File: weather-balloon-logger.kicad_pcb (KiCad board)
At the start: 2 copper layers, 30 x 20 mm, 0 parts

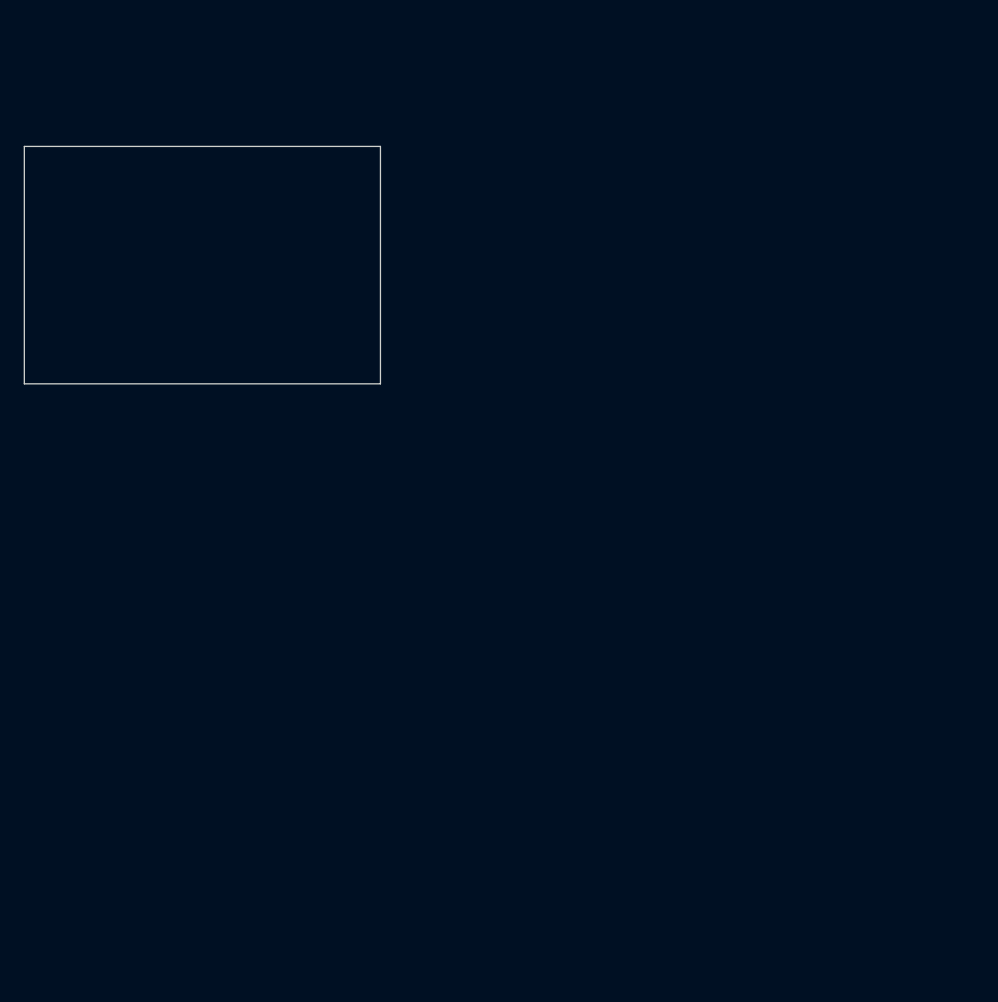
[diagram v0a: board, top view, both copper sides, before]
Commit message: copperhead: create pipeline stage: layout-draft
Completed pipeline stage layout-draft. The 80 × 70 mm PCB contains explicit coordinates for all 15 refdes, edge-located connectors, local OpenLog decoupling, compact LED and cutdown clusters, dual 5 mm SMA clearance envelopes, reserved ESD areas, and DRC-clean routing for power, ground, RF, UART/LED, decoupling, and cutdown nets. LAYOUT.md includes the required `## Draft quality` section with precise acceptable work and mandatory specialist rework. Final verification: ERC clean, DRC clean, BOM/PINOUT drift clean, and board SVG exported. Pre-fabrication holds remain explicitly documented: replace board-local placeholder land patterns, enforce RF rule areas, design 50 Ω launches from a real stackup, capture qualified ESD parts, and complete mechanical/thermal review.

Verification: ERC clean, DRC clean
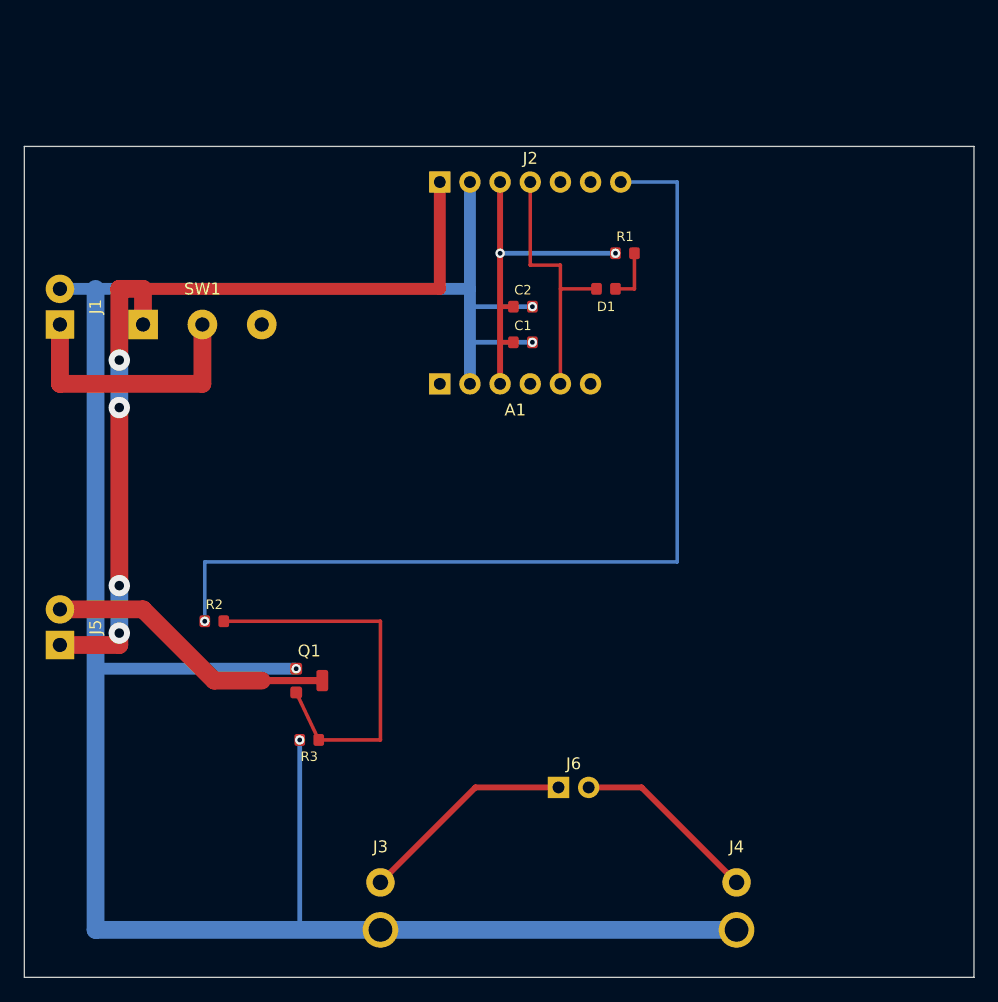
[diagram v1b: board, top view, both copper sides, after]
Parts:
- added A1: OpenLog, CopperheadDraft_PinSocket_1x06_P2.54mm_Vertical, F.Cu at (135.0, 120.0)
- added C1: 4.7uF, CopperheadDraft_C_0603_1608Metric, F.Cu at (142.0, 116.5)
- added C2: 100nF, CopperheadDraft_C_0603_1608Metric, F.Cu at (142.0, 113.5)
- added D1: LTST-C190KGKT, CopperheadDraft_LED_0603_1608Metric, F.Cu at (149.0, 112.0)
- added J1: Conn_01x02, CopperheadDraft_Molex_Micro-Fit_3.0_43650-0200_1x02_P3.00mm_Horizontal, F.Cu at (103.0, 115.0)
- added J2: Conn_01x07, CopperheadDraft_PinHeader_1x07_P2.54mm_Vertical, F.Cu at (135.0, 103.0)
- added J3: SMA, CopperheadDraft_SMA_Amphenol_132289, F.Cu at (130.0, 162.0)
- added J4: SMA, CopperheadDraft_SMA_Amphenol_132289, F.Cu at (160.0, 162.0)
- added J5: Conn_01x02, CopperheadDraft_Molex_Micro-Fit_3.0_43650-0200_1x02_P3.00mm_Horizontal, F.Cu at (103.0, 142.0)
- added J6: Conn_01x02, CopperheadDraft_PinHeader_1x02_P2.54mm_Vertical, F.Cu at (145.0, 154.0)
- added Q1: AO3400A, CopperheadDraft_SOT-23, F.Cu at (124.0, 145.0)
- added R1: 1k, CopperheadDraft_R_0603_1608Metric, F.Cu at (150.6, 109.0)
- added R2: 100R, CopperheadDraft_R_0603_1608Metric, F.Cu at (116.0, 140.0)
- added R3: 1M, CopperheadDraft_R_0603_1608Metric, F.Cu at (124.0, 150.0)
- added SW1: SPDT, CopperheadDraft_SW_CK_7101MD9CQE, F.Cu at (115.0, 115.0)
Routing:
- net GND: track 0.00 -> 203.0 mm, vias 0 -> 4
- net CUTDOWN_CTRL: track 0.00 -> 81.6 mm, vias 0 -> 1
- net PACK_SW: track 0.00 -> 74.0 mm, vias 0 -> 4
- net CUTDOWN_GATE: track 0.00 -> 32.8 mm
- net 3V3: track 0.00 -> 29.0 mm, vias 0 -> 2
- net CUTDOWN_DRAIN: track 0.00 -> 24.6 mm
- net UART_TX: track 0.00 -> 22.6 mm
- net PACK_IN: track 0.00 -> 22.0 mm
- net RF_APRS: track 0.00 -> 18.3 mm
- net RF_WSPR: track 0.00 -> 15.8 mm
- net LED_A: track 0.00 -> 4.60 mm
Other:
- board size 30 x 20 mm -> 80 x 70 mm
- board text added: "APRS 5mm RF CLEARANCE"
- board text added: "RESERVED ESD"
- board text added: "WSPR 5mm RF CLEARANCE"

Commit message: copperhead: Re-lay-out the board for the revised schematic and reserve a 32 x 55 mm LightAPRS-W 2.0 module-mount zone per docs/SUBSYSTEMS.md section 6. Place the mating headers J2 (11-pin host interface), J6 (VHF) and J7 (HF) INSIDE that zone, positioned to align with the module's 2.54 mm edge header and its bottom opposite-corner HF/VHF pins so the module plugs directly onto them; add corner standoff mounting holes in the zone. Place all OTHER components (J1 pack input, SW1, A1 OpenLog, U1 PCF8574T + C3, J3/J4 SMA jacks, Q1 cutdown plus D1/R1/R2/R3/C1/C2) OUTSIDE the module footprint so they cannot collide with the module body, honoring the >=5 mm SMA keepouts. Update docs/LAYOUT.md and the board, then re-run DRC.
Re-laid out the 80 x 70 mm PCB for the revised 18-refdes schematic; added the explicit 32 x 55 mm LightAPRS-W zone at (124,101)-(156,156), placed J2/J6/J7 and four approximate M2 standoff holes inside it, kept all other electrical components outside, retained separate >=5 mm SMA clearance intent, routed the revised UART/I2C/LED/cutdown/RF nets, and updated LAYOUT, SUBSYSTEMS, CHANGELOG, decisions, and constraints. Final ERC clean, DRC clean, drift clean, and board SVG exported. Existing outputs remain stale and fabrication remains blocked pending physical module geometry, exact footprint, RF, thermal, leakage, and sourcing verification.

Verification: ERC clean, DRC clean
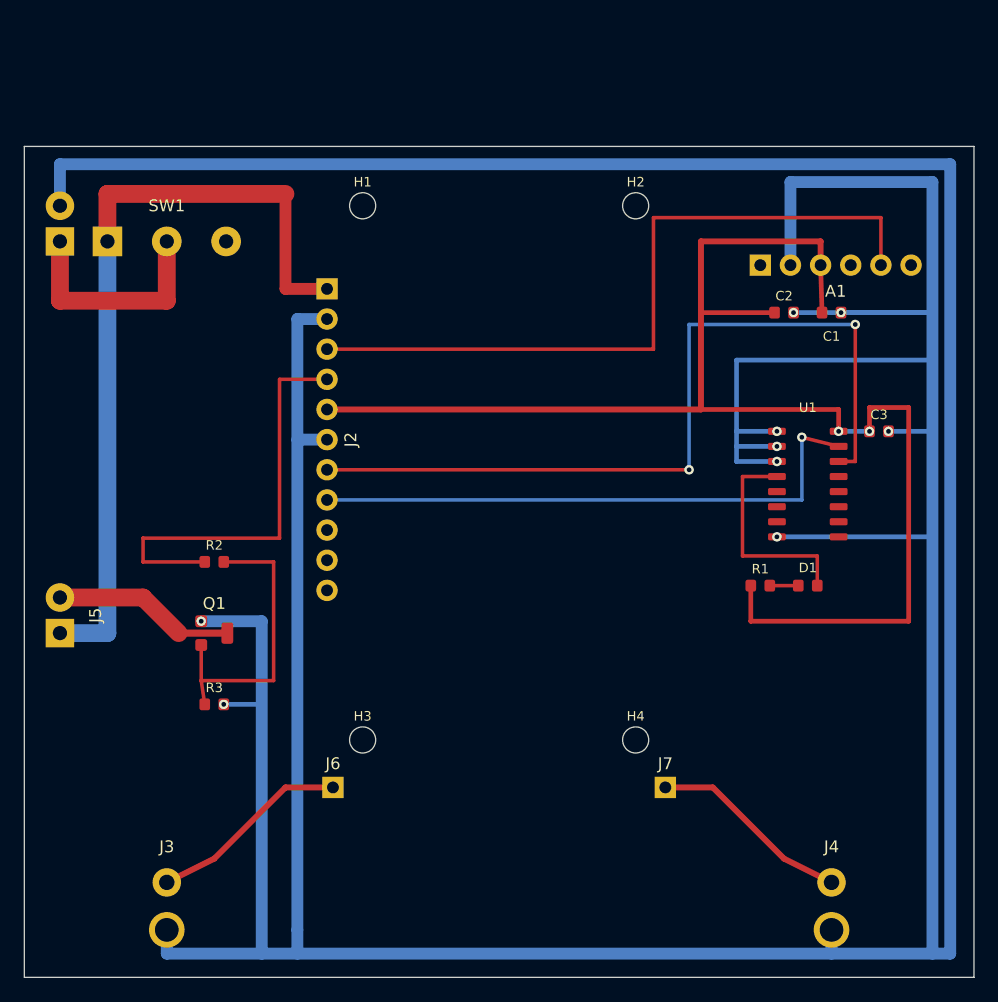
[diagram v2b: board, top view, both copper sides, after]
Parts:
- added C3: 100nF, CopperheadDraft_C_0603_1608Metric, F.Cu at (172.0, 124.0)
- added H1: M2_STANDOFF, CopperheadDraft_MountingHole_2.2mm, F.Cu at (128.5, 105.0)
- added H2: M2_STANDOFF, CopperheadDraft_MountingHole_2.2mm, F.Cu at (151.5, 105.0)
- added H3: M2_STANDOFF, CopperheadDraft_MountingHole_2.2mm, F.Cu at (128.5, 150.0)
- added H4: M2_STANDOFF, CopperheadDraft_MountingHole_2.2mm, F.Cu at (151.5, 150.0)
- added J7: HF, CopperheadDraft_PinHeader_1x01_P2.54mm_Vertical, F.Cu at (154.0, 154.0)
- added U1: PCF8574T, CopperheadDraft_SOIC-16_3.9x9.9mm_P1.27mm, F.Cu at (166.0, 128.0)
- J2: value Conn_01x07 -> Conn_01x11; footprint CopperheadDraft_PinHeader_1x07_P2.54mm_Vertical -> CopperheadDraft_PinHeader_1x11_P2.54mm_Vertical
- J6: value Conn_01x02 -> VHF; footprint CopperheadDraft_PinHeader_1x02_P2.54mm_Vertical -> CopperheadDraft_PinHeader_1x01_P2.54mm_Vertical
- moved D1 30.2 mm to (166.0, 137.0), turned to 180 degrees
- moved R1 30.2 mm to (162.0, 137.0)
- moved A1 28.8 mm to (162.0, 110.0)
- moved C1 26.1 mm to (168.0, 114.0)
- moved C2 22.0 mm to (164.0, 114.0)
- moved J6 19.0 mm to (126.0, 154.0)
- moved J3 18.0 mm to (112.0, 162.0)
- moved J2 13.1 mm to (125.5, 112.0), turned to 270 degrees
- moved Q1 8.94 mm to (116.0, 141.0)
- moved R3 8.54 mm to (116.0, 147.0), turned to 0 degrees
- moved J4 8.00 mm to (168.0, 162.0)
- moved SW1 7.62 mm to (112.0, 108.0)
- moved J1 7.00 mm to (103.0, 108.0)
- moved R2 5.00 mm to (116.0, 135.0)
- moved J5 1.00 mm to (103.0, 141.0)
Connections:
- D1 pad 1: UART_TX -> LED_N
- J2 pad 3: 3V3 -> UART_TX
- J2 pad 4: UART_TX -> CUTDOWN_CTRL
- J2 pad 5: (no net) -> 3V3
- J2 pad 6: (no net) -> GND
- J2 pad 7: CUTDOWN_CTRL -> I2C_SCL
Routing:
- net GND: track 203.0 -> 465.2 mm, vias 4 -> 9
- net 3V3: track 29.0 -> 123.6 mm
- net I2C_SCL: track 0.00 -> 69.7 mm, vias 0 -> 2
- net I2C_SDA: track 0.00 -> 48.5 mm, vias 0 -> 1
- net CUTDOWN_CTRL: track 81.6 -> 36.1 mm, vias 1 -> 0
- net UART_TX: track 22.6 -> 61.7 mm
- net LED_N: track 0.00 -> 18.4 mm
- net CUTDOWN_DRAIN: track 24.6 -> 15.3 mm
- net CUTDOWN_GATE: track 32.8 -> 25.3 mm
- net PACK_SW: track 74.0 -> 67.5 mm, vias 4 -> 0
- net PACK_IN: track 22.0 -> 19.0 mm
- net LED_A: track 4.60 -> 2.40 mm
- net RF_APRS: track 18.3 -> 17.0 mm
- net RF_WSPR: track 15.8 -> 17.0 mm
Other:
- board text added: "LIGHTAPRS-W 2.0 MODULE ZONE 32 x 55 mm"
